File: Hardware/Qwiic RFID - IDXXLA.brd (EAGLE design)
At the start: 25.4 x 30.5 mm, 60 parts, among them J2 SMD, J3 PTH, J4 SMD, J8 AVR_SPI_PROG_3X2TESTPOINTS, Q1 600mA/40V, U1 ATTINY84-ARDUINO, U2 ID-12/20SMD

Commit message: Panel for x02
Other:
- board text added: "X02"
- board text removed: "X01"
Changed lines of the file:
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@@
 <wire x1="25.4" y1="30.48" x2="25.4" y2="0" width="0.2032" layer="20"/>
 <wire x1="25.4" y1="0" x2="0" y2="0" width="0.2032" layer="20"/>
-<text x="17.653" y="29.21" size="1.27" layer="16" font="vector" ratio="15" rot="MR0" align="center">X01</text>
+<text x="17.653" y="29.21" size="1.27" layer="16" font="vector" ratio="15" rot="MR0" align="center">X02</text>
 <text x="1.27" y="38.1" size="1.778" layer="47" font="vector" ratio="15">Units in Inches</text>
 <text x="21.59" y="-10.16" size="1.778" layer="51" font="vector" ratio="15">Elias Santistevan</text>

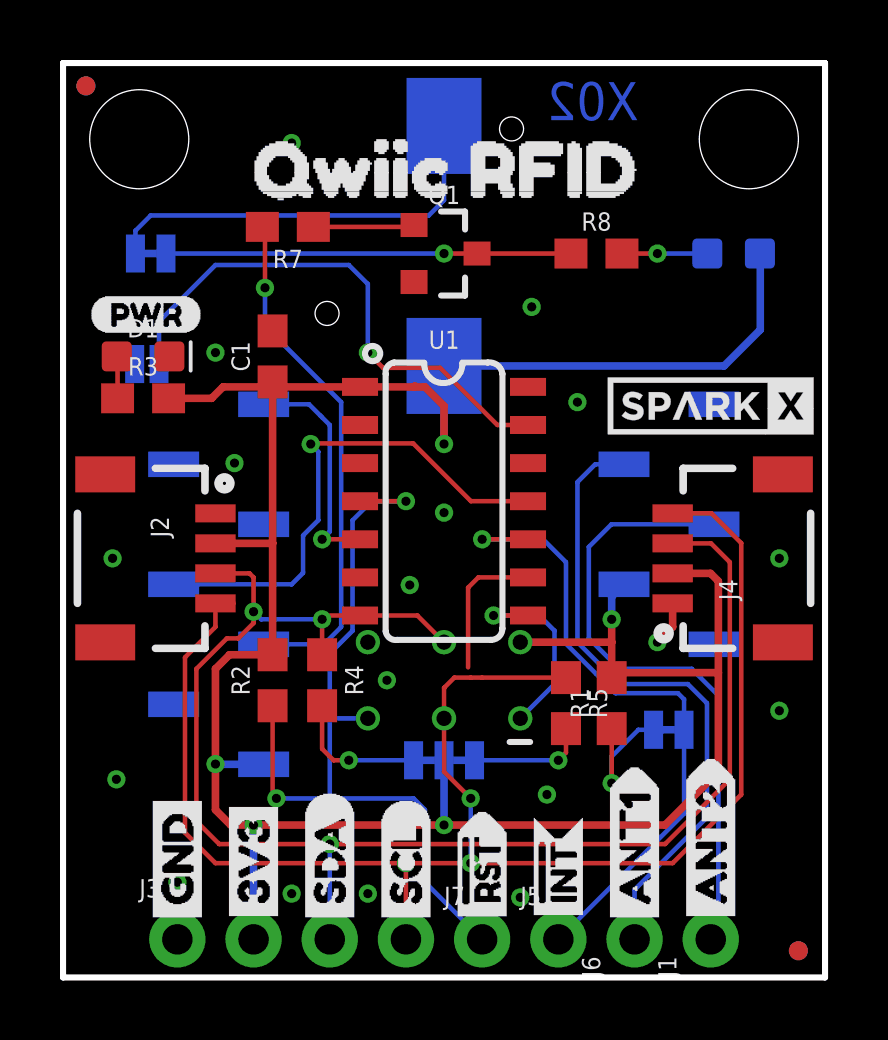
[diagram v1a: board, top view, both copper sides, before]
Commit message: Fixed DRC erros added latest panel for x02
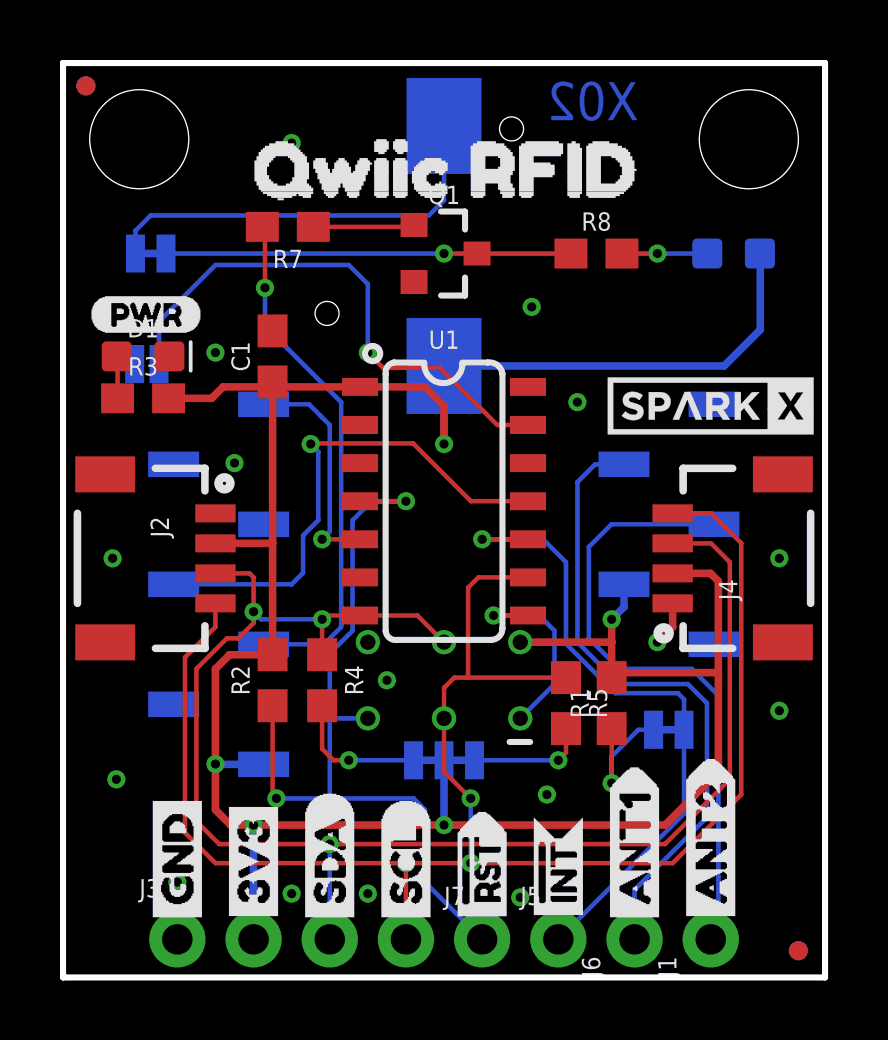
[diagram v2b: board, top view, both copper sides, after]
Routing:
- net SDA/MOSI: track 50.6 -> 50.1 mm
- net GND: vias 18 -> 16
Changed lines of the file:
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@@
 <wire x1="5.0884" y1="7.1036" x2="5.08" y2="7.112" width="0.254" layer="16"/>
 <via x="5.08" y="7.112" extent="1-16" drill="0.3048"/>
-<wire x1="18.6756" y1="13.081" x2="18.6982" y2="13.1036" width="0.254" layer="16"/>
 <via x="12.7" y="17.78" extent="1-16" drill="0.3048"/>
 <wire x1="12.7" y1="20.384" x2="12.7" y2="17.78" width="0.254" layer="16"/>
 <wire x1="12.7" y1="17.78" x2="12.7" y2="19.05" width="0.254" layer="1"/>
 <wire x1="12.7" y1="19.05" x2="12.065" y2="19.685" width="0.254" layer="1"/>
-<wire x1="12.065" y1="19.685" x2="11.684" y2="19.685" width="0.254" layer="1"/>
-<wire x1="11.684" y1="19.685" x2="9.9" y2="19.685" width="0.254" layer="1"/>
 <wire x1="20.32" y1="13.47" x2="21.582" y2="13.47" width="0.254" layer="1"/>
 <wire x1="21.582" y1="13.47" x2="21.844" y2="13.208" width="0.254" layer="1"/>
@@
 <wire x1="23.241" y1="24.118" x2="23.229" y2="24.13" width="0.254" layer="16"/>
 <wire x1="23.241" y1="21.59" x2="23.241" y2="24.118" width="0.254" layer="16"/>
-<wire x1="18.6982" y1="13.1036" x2="18.288" y2="12.6934" width="0.254" layer="16"/>
-<wire x1="18.288" y1="12.6934" x2="18.288" y2="11.938" width="0.254" layer="16"/>
 <via x="18.288" y="11.938" extent="1-16" drill="0.3048"/>
 <wire x1="5.08" y1="7.112" x2="5.08" y2="10.287" width="0.254" layer="1"/>
@@
 <wire x1="3.517" y1="19.304" x2="4.953" y2="19.304" width="0.254" layer="1"/>
 <contactref element="C1" pad="1"/>
-<wire x1="11.723" y1="19.724" x2="11.684" y2="19.685" width="0.254" layer="1"/>
-<wire x1="9.861" y1="19.646" x2="9.9" y2="19.685" width="0.254" layer="1"/>
 <wire x1="5.08" y1="5.588" x2="5.588" y2="5.08" width="0.254" layer="1"/>
 <wire x1="5.08" y1="7.112" x2="5.08" y2="5.588" width="0.254" layer="1"/>
@@
 <wire x1="12.7" y1="20.384" x2="22.035" y2="20.384" width="0.254" layer="16"/>
 <wire x1="22.035" y1="20.384" x2="23.241" y2="21.59" width="0.254" layer="16"/>
+<wire x1="12.065" y1="19.685" x2="9.9" y2="19.685" width="0.254" layer="1"/>
+<wire x1="18.288" y1="11.938" x2="18.6982" y2="12.3482" width="0.254" layer="16"/>
+<wire x1="18.6982" y1="12.3482" x2="18.6982" y2="13.1036" width="0.254" layer="16"/>
 </signal>
 <signal name="GND">
@@
 <via x="16.129" y="6.096" extent="1-16" drill="0.3048"/>
 <via x="15.621" y="22.352" extent="1-16" drill="0.3048"/>
-<via x="12.7" y="15.494" extent="1-16" drill="0.3048"/>
 <via x="17.145" y="19.177" extent="1-16" drill="0.3048"/>
 <via x="23.876" y="13.97" extent="1-16" drill="0.3048"/>
 <via x="3.81" y="3.175" extent="1-16" drill="0.3048"/>
 <via x="10.795" y="9.906" extent="1-16" drill="0.3048"/>
-<via x="11.557" y="13.081" extent="1-16" drill="0.3048"/>
 <via x="1.778" y="6.604" extent="1-16" drill="0.3048"/>
 <via x="1.651" y="13.97" extent="1-16" drill="0.3048"/>
@@
 <wire x1="13.843" y1="13.335" x2="15.5" y2="13.335" width="0.1524" layer="1"/>
 <contactref element="J2" pad="4"/>
-<wire x1="5.08" y1="12.47" x2="5.691" y2="12.47" width="0.1524" layer="1"/>
 <contactref element="J3" pad="4"/>
 <contactref element="J4" pad="4"/>
@@
 <wire x1="13.589" y1="5.969" x2="13.589" y2="3.81" width="0.1524" layer="16"/>
 <via x="13.589" y="3.81" extent="1-16" drill="0.3048"/>
-<wire x1="5.08" y1="11.684" x2="5.08" y2="12.47" width="0.1524" layer="1"/>
 <wire x1="12.7" y1="8.636" x2="12.7" y2="6.858" width="0.1524" layer="1"/>
 <wire x1="12.7" y1="6.858" x2="13.589" y2="5.969" width="0.1524" layer="1"/>
 <wire x1="12.7" y1="8.636" x2="12.7" y2="9.652" width="0.1524" layer="1"/>
 <wire x1="12.7" y1="9.652" x2="13.042" y2="9.994" width="0.1524" layer="1"/>
-<wire x1="13.042" y1="9.994" x2="13.589" y2="9.994" width="0.1524" layer="1"/>
-<wire x1="13.589" y1="9.994" x2="13.97" y2="9.994" width="0.1524" layer="1"/>
-<wire x1="13.97" y1="9.994" x2="16.764" y2="9.994" width="0.1524" layer="1"/>
-<wire x1="13.501" y1="12.993" x2="13.501" y2="10.336" width="0.1524" layer="1"/>
-<wire x1="13.589" y1="9.994" x2="13.501" y2="10.336" width="0" layer="19" extent="1-1"/>
+<wire x1="13.042" y1="9.994" x2="13.462" y2="9.994" width="0.1524" layer="1"/>
+<wire x1="13.462" y1="9.994" x2="16.764" y2="9.994" width="0.1524" layer="1"/>
+<wire x1="13.501" y1="10.033" x2="13.462" y2="9.994" width="0.1524" layer="1"/>
+<wire x1="13.501" y1="12.993" x2="13.501" y2="10.033" width="0.1524" layer="1"/>
+<wire x1="5.08" y1="11.684" x2="5.08" y2="12.47" width="0.1524" layer="1"/>
 </signal>
 <signal name="SDA/MOSI">
@@
 <contactref element="J3" pad="3"/>
 <contactref element="J4" pad="3"/>
-<wire x1="5.08" y1="13.47" x2="5.58" y2="13.47" width="0.1524" layer="1"/>
-<wire x1="5.088" y1="13.462" x2="5.08" y2="13.47" width="0.1524" layer="1"/>
 <wire x1="22.225" y1="6.604" x2="22.225" y2="13.843" width="0.1524" layer="1"/>
 <wire x1="20.32" y1="14.47" x2="21.598" y2="14.47" width="0.1524" layer="1"/>
@@
 <wire x1="20.066" y1="4.445" x2="22.225" y2="6.604" width="0.1524" layer="1"/>
 <wire x1="8.89" y1="4.445" x2="20.066" y2="4.445" width="0.1524" layer="1"/>
-<wire x1="5.08" y1="13.47" x2="6.215" y2="13.47" width="0.1524" layer="1"/>
-<wire x1="6.215" y1="13.47" x2="6.35" y2="13.335" width="0.1524" layer="1"/>
+<wire x1="6.35" y1="13.335" x2="6.215" y2="13.47" width="0.1524" layer="1"/>
 <wire x1="6.35" y1="13.335" x2="6.35" y2="12.192" width="0.1524" layer="1"/>
 <wire x1="8.89" y1="4.445" x2="5.207" y2="4.445" width="0.1524" layer="1"/>
@@
 <wire x1="5.842" y1="11.303" x2="6.35" y2="11.811" width="0.1524" layer="1"/>
 <wire x1="6.35" y1="11.811" x2="6.35" y2="12.192" width="0.1524" layer="1"/>
+<wire x1="6.215" y1="13.47" x2="5.08" y2="13.47" width="0.1524" layer="1"/>
 </signal>
 <signal name="!RST">
@@
 <wire x1="18.288" y1="8.294" x2="18.288" y2="6.477" width="0.1524" layer="1"/>
 <via x="18.288" y="6.477" extent="1-16" drill="0.3048"/>
-<wire x1="18.288" y1="6.477" x2="18.288" y2="6.858" width="0.1524" layer="16"/>
-<wire x1="19.177" y1="8.255" x2="18.288" y2="7.366" width="0.1524" layer="16"/>
-<wire x1="18.288" y1="7.366" x2="18.288" y2="6.477" width="0.1524" layer="16"/>
+<wire x1="18.288" y1="7.366" x2="19.177" y2="8.255" width="0.1524" layer="16"/>
+<wire x1="18.288" y1="6.477" x2="18.288" y2="7.366" width="0.1524" layer="16"/>
 </signal>
 <signal name="DATA_UART">

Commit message: Cleanup and ReadMe
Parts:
- J2, J4: value SMD -> (none); device SparkX:1X04_1MM_RA -> SparkFun-Connectors:1X04_1MM_RA
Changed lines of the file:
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@@
 </element>
 <element name="I2C" library="SparkFun-Jumpers" package="SMT-JUMPER_3_2-NC_TRACE_SILK" value="" x="12.7" y="7.239" rot="MR0"/>
-<element name="J2" library="SparkX" package="1X04_1MM_RA" value="SMD" x="5.08" y="13.97" rot="R270"/>
+<element name="J2" library="SparkFun-Connectors" package="1X04_1MM_RA" value="" x="5.08" y="13.97" rot="R270">
+<attribute name="PROD_ID" value="CONN-13694" x="5.08" y="13.97" size="1.778" layer="27" rot="R270" display="off"/>
+<attribute name="VALUE" value="" x="5.08" y="13.97" size="1.778" layer="27" rot="R270" display="off"/>
+</element>
 <element name="J3" library="SparkX" package="1X04_NO_SILK" value="PTH" x="3.81" y="1.27"/>
 <element name="FRAME1" library="SparkFun-Aesthetics" package="CREATIVE_COMMONS" value="FRAME-LETTER" x="-8.89" y="-10.16"/>
-<element name="J4" library="SparkX" package="1X04_1MM_RA" value="SMD" x="20.32" y="13.97" rot="R90"/>
+<element name="J4" library="SparkFun-Connectors" package="1X04_1MM_RA" value="" x="20.32" y="13.97" rot="R90">
+<attribute name="PROD_ID" value="CONN-13694" x="20.32" y="13.97" size="1.778" layer="27" rot="R90" display="off"/>
+<attribute name="VALUE" value="" x="20.32" y="13.97" size="1.778" layer="27" rot="R90" display="off"/>
+</element>
 <element name="LOGO1" library="SparkFun-Aesthetics" package="OSHW-LOGO-MINI" value="OSHW-LOGOMINI" x="18.923" y="28.575" rot="MR0"/>
 <element name="J5" library="SparkFun-Connectors" package="1X01_NO_SILK" value="" x="16.51" y="1.27"/>
